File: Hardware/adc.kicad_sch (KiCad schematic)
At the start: 14 parts, among them U2 NAU7802SGI, Y1 Crystal_GND23

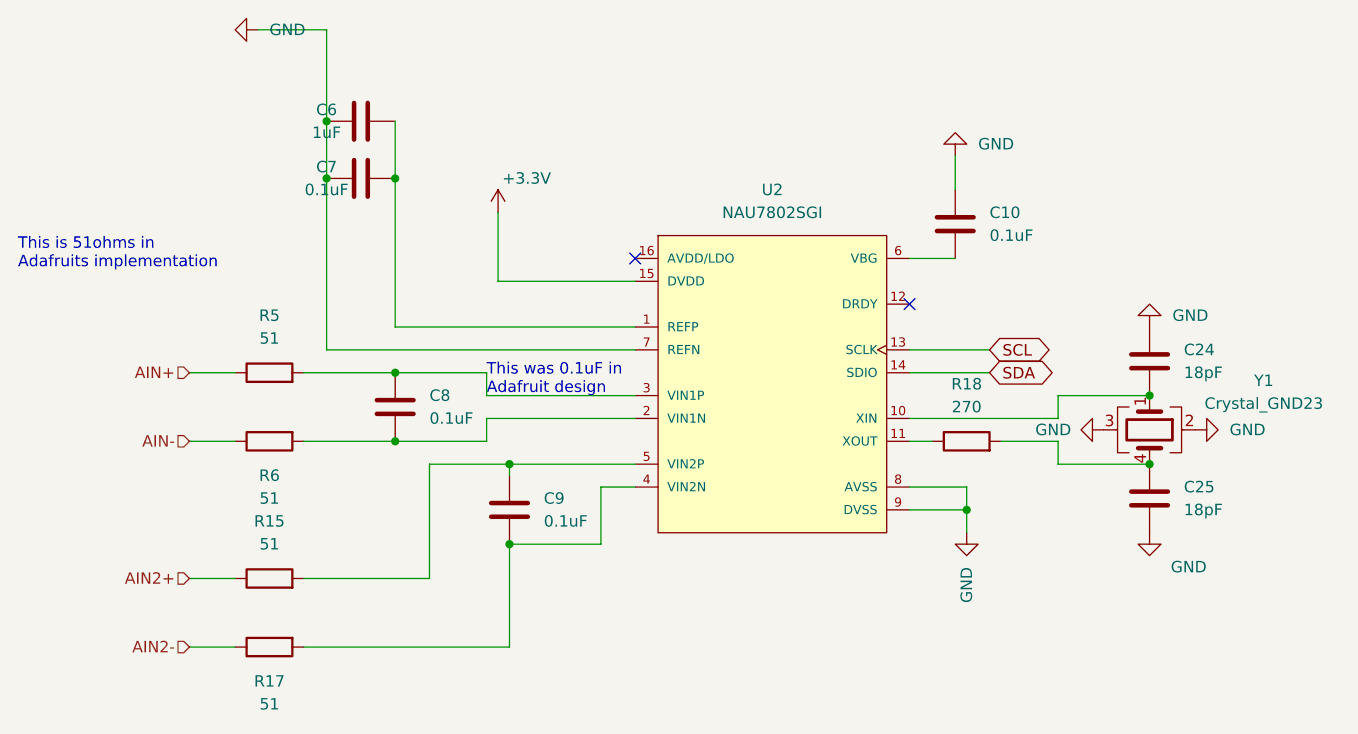
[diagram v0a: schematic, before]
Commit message: removed 2.5v circuit to use the built in variable ldo on the ADC added ~4.915Mhz crystal for 50/60Hz filtering fixed several small schematic issues completely relaid out the board.
Signed-off-by: lokimetasmith <lokimail@gmail.com>
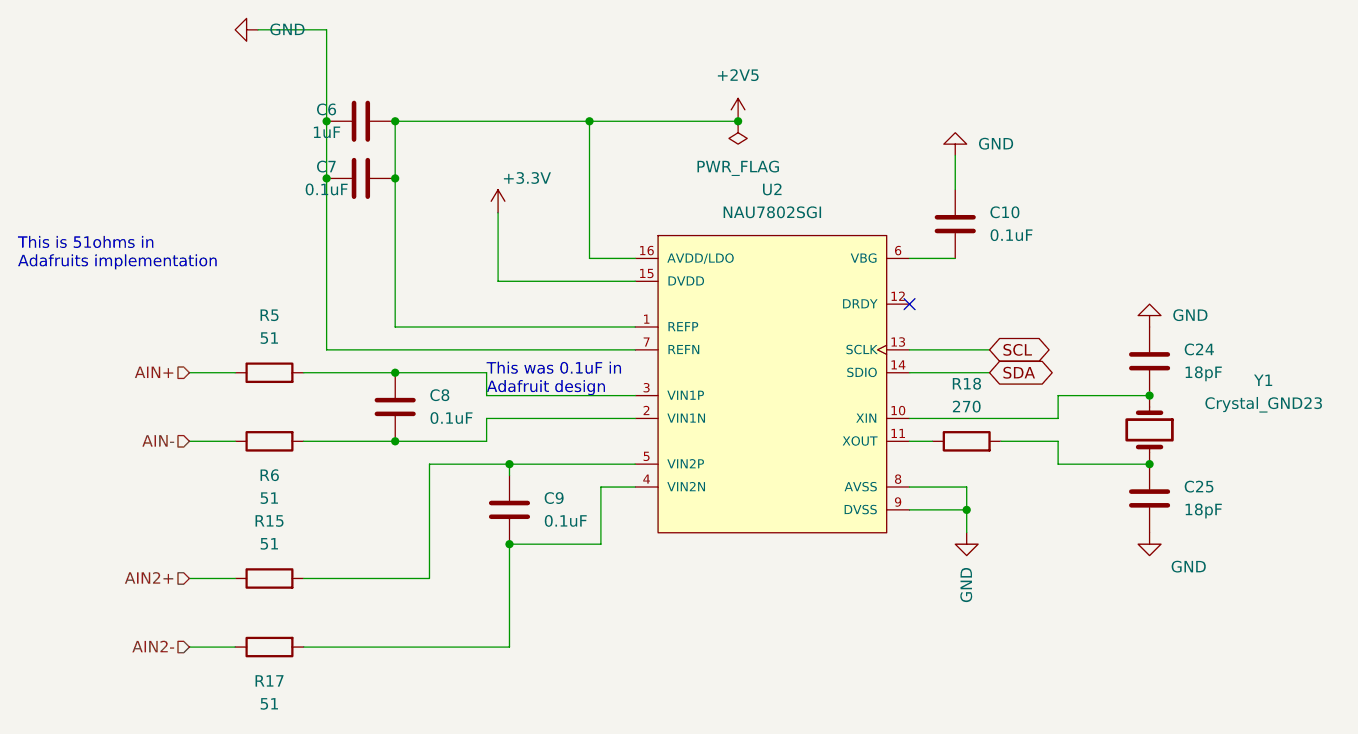
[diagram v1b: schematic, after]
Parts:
- Y1: footprint Crystal:Crystal_SMD_3225-4Pin_3.2x2.5mm_HandSoldering -> Crystal:Crystal_SMD_HC49-SD; symbol Device:Crystal_GND23 -> Device:Crystal
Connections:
- net GND: no longer Y1.2, Y1.3
- net +2V5: now reaches C6.2, C7.2, U2.1 (REFP)
- net +2V5: now also U2.16 (AVDD/LDO)
- net at C25.1, R18.2: now also Y1.2; no longer Y1.4
- no-connect marks 2 -> 1
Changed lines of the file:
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@@
   (junction (at 115.57 88.9) (diameter 0) (color 0 0 0 0)
   )
+  (junction (at 137.16 82.55) (diameter 0) (color 0 0 0 0)
+  )
+  (junction (at 115.57 82.55) (diameter 0) (color 0 0 0 0)
+  )
   (junction (at 115.57 110.49) (diameter 0) (color 0 0 0 0)
   )
+  (junction (at 153.67 82.55) (diameter 0) (color 0 0 0 0)
+  )
   (junction (at 199.39 120.65) (diameter 0) (color 0 0 0 0)
   )
@@
   )
   (no_connect (at 172.72 102.87))
-  (no_connect (at 142.24 97.79))
+  (wire (pts (xy 137.16 82.55) (xy 137.16 97.79))
+    (stroke (width 0) (type default) (color 0 0 0 0))
+  )
   (wire (pts (xy 100.33 72.39) (xy 107.95 72.39))
     (stroke (width 0) (type default) (color 0 0 0 0))
@@
     (stroke (width 0) (type default) (color 0 0 0 0))
   )
+  (wire (pts (xy 115.57 82.55) (xy 137.16 82.55))
+    (stroke (width 0) (type default) (color 0 0 0 0))
+  )
   (wire (pts (xy 92.71 140.97) (xy 97.79 140.97))
     (stroke (width 0) (type default) (color 0 0 0 0))
@@
     (stroke (width 0) (type default) (color 0 0 0 0))
   )
+  (wire (pts (xy 137.16 82.55) (xy 153.67 82.55))
+    (stroke (width 0) (type default) (color 0 0 0 0))
+  )
   (wire (pts (xy 107.95 107.95) (xy 107.95 88.9))
     (stroke (width 0) (type default) (color 0 0 0 0))
@@
   )
   (wire (pts (xy 125.73 115.57) (xy 125.73 118.11))
+    (stroke (width 0) (type default) (color 0 0 0 0))
+  )
+  (wire (pts (xy 137.16 97.79) (xy 142.24 97.79))
     (stroke (width 0) (type default) (color 0 0 0 0))
   )
@@
     (pin "9")
   )
+  (symbol (lib_id "power:PWR_FLAG") (at 153.67 82.55 0) (mirror x) (unit 1)
+    (in_bom yes) (on_board yes) (fields_autoplaced)
+    (property "Reference" "#FLG0101" (id 0) (at 153.67 84.455 0)
+      (effects (font (size 1.27 1.27)) hide)
+    )
+    (property "Value" "PWR_FLAG" (id 1) (at 153.67 87.63 0))
+    (property "Footprint" "" (id 2) (at 153.67 82.55 0)
+      (effects (font (size 1.27 1.27)) hide)
+    )
+    (property "Datasheet" "~" (id 3) (at 153.67 82.55 0)
+      (effects (font (size 1.27 1.27)) hide)
+    )
+    (pin "1")
+  )
   (symbol (lib_id "Device:C") (at 111.76 88.9 90) (unit 1)
     (in_bom yes) (on_board yes)
@@
     (pin "1")
   )
-  (symbol (lib_id "power:GND") (at 204.47 116.84 90) (unit 1)
-    (in_bom yes) (on_board yes) (fields_autoplaced)
-    (property "Reference" "#PWR013" (id 0) (at 210.82 116.84 0)
-      (effects (font (size 1.27 1.27)) hide)
-    )
-    (property "Value" "GND" (id 1) (at 208.28 116.8399 90)
-      (effects (font (size 1.27 1.27)) (justify right))
-    )
-    (property "Footprint" "" (id 2) (at 204.47 116.84 0)
-      (effects (font (size 1.27 1.27)) hide)
-    )
-    (property "Datasheet" "" (id 3) (at 204.47 116.84 0)
-      (effects (font (size 1.27 1.27)) hide)
-    )
-    (pin "1")
-  )
   (symbol (lib_id "Device:C") (at 128.27 125.73 0) (unit 1)
     (in_bom yes) (on_board yes)
@@
     (pin "2")
   )
-  (symbol (lib_id "Device:Crystal_GND23") (at 199.39 116.84 270) (unit 1)
+  (symbol (lib_id "Device:Crystal") (at 199.39 116.84 270) (unit 1)
     (in_bom yes) (on_board yes) (fields_autoplaced)
     (property "Reference" "Y1" (id 0) (at 212.09 111.3788 90))
     (property "Value" "Crystal_GND23" (id 1) (at 212.09 113.9188 90))
-    (property "Footprint" "Crystal:Crystal_SMD_3225-4Pin_3.2x2.5mm_HandSoldering" (id 2) (at 199.39 116.84 0)
+    (property "Footprint" "Crystal:Crystal_SMD_HC49-SD" (id 2) (at 199.39 116.84 0)
       (effects (font (size 1.27 1.27)) hide)
     )
@@
     (pin "1")
     (pin "2")
-    (pin "3")
-    (pin "4")
   )
   (symbol (lib_id "power:GND") (at 100.33 72.39 270) (unit 1)
@@
     (pin "1")
   )
+  (symbol (lib_id "power:+2V5") (at 153.67 82.55 0) (unit 1)
+    (in_bom yes) (on_board yes) (fields_autoplaced)
+    (property "Reference" "#PWR0118" (id 0) (at 153.67 86.36 0)
+      (effects (font (size 1.27 1.27)) hide)
+    )
+    (property "Value" "+2V5" (id 1) (at 153.67 77.47 0))
+    (property "Footprint" "" (id 2) (at 153.67 82.55 0)
+      (effects (font (size 1.27 1.27)) hide)
+    )
+    (property "Datasheet" "" (id 3) (at 153.67 82.55 0)
+      (effects (font (size 1.27 1.27)) hide)
+    )
+    (pin "1")
+  )
   (symbol (lib_id "Device:C") (at 115.57 114.3 0) (unit 1)
     (in_bom yes) (on_board yes) (fields_autoplaced)
@@
     (pin "2")
   )
-  (symbol (lib_id "power:GND") (at 194.31 116.84 270) (unit 1)
-    (in_bom yes) (on_board yes)
-    (property "Reference" "#PWR010" (id 0) (at 187.96 116.84 0)
-      (effects (font (size 1.27 1.27)) hide)
-    )
-    (property "Value" "GND" (id 1) (at 186.69 116.84 90)
-      (effects (font (size 1.27 1.27)) (justify left))
-    )
-    (property "Footprint" "" (id 2) (at 194.31 116.84 0)
-      (effects (font (size 1.27 1.27)) hide)
-    )
-    (property "Datasheet" "" (id 3) (at 194.31 116.84 0)
-      (effects (font (size 1.27 1.27)) hide)
-    )
-    (pin "1")
-  )
   (symbol (lib_id "Device:R") (at 101.6 118.11 90) (mirror x) (unit 1)
